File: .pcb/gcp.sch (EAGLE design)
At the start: 14 parts, among them SW1 POWER/COFFEE_SWITCHON-OFF

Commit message: Fixed steam lamp circuitry
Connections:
- net GREY: no longer STEAM_LAMP.2
- net N$2: now also STEAM_LAMP.2
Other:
- moved on the sheet: SSR-40DA1, STEAM_LAMP
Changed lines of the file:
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@@
 <attribute name="VALUE" x="-294.64" y="-64.77" size="1.778" layer="96" rot="R180"/>
 </instance>
-<instance part="STEAM_LAMP" gate="G$1" x="-274.32" y="-2.54" smashed="yes" rot="R90">
-<attribute name="NAME" x="-278.765" y="-5.08" size="1.778" layer="95" rot="R90"/>
-<attribute name="VALUE" x="-267.97" y="-5.08" size="1.778" layer="96" rot="R90"/>
+<instance part="STEAM_LAMP" gate="G$1" x="-231.14" y="0" smashed="yes" rot="R90">
+<attribute name="NAME" x="-235.585" y="-2.54" size="1.778" layer="95" rot="R90"/>
+<attribute name="VALUE" x="-224.79" y="-2.54" size="1.778" layer="96" rot="R90"/>
 </instance>
 <instance part="PUMP" gate="G$1" x="-187.96" y="5.08" smashed="yes" rot="R90">
@@
 <attribute name="VALUE" x="-215.9" y="22.86" size="1.778" layer="96" rot="R90"/>
 </instance>
-<instance part="SSR-40DA1" gate="G$1" x="-251.46" y="7.62" smashed="yes" rot="R90">
-<attribute name="NAME" x="-257.81" y="0" size="1.778" layer="95" font="vector" rot="R90"/>
+<instance part="SSR-40DA1" gate="G$1" x="-246.38" y="7.62" smashed="yes" rot="R90">
+<attribute name="NAME" x="-252.73" y="0" size="1.778" layer="95" font="vector" rot="R90"/>
 </instance>
 </instances>
@@
 <segment>
 <pinref part="SSR-40DA1" gate="G$1" pin="K"/>
-<wire x1="-248.92" y1="-2.54" x2="-248.92" y2="-5.08" width="0.1524" layer="91"/>
-<label x="-248.92" y="-5.08" size="1.778" layer="95" rot="R270"/>
+<wire x1="-243.84" y1="-2.54" x2="-243.84" y2="-5.08" width="0.1524" layer="91"/>
+<label x="-243.84" y="-5.08" size="1.778" layer="95" rot="R270"/>
 </segment>
 </net>
@@
 <segment>
 <pinref part="STEAM_LAMP" gate="G$1" pin="1"/>
-<wire x1="-274.32" y1="-15.24" x2="-274.32" y2="-7.62" width="0.1524" layer="91"/>
+<wire x1="-231.14" y1="-15.24" x2="-231.14" y2="-5.08" width="0.1524" layer="91"/>
 <pinref part="HEATER2" gate="G$1" pin="P$2"/>
-<wire x1="-261.62" y1="-15.24" x2="-274.32" y2="-15.24" width="0.1524" layer="91"/>
+<wire x1="-261.62" y1="-15.24" x2="-231.14" y2="-15.24" width="0.1524" layer="91"/>
 <wire x1="-254" y1="-27.94" x2="-254" y2="-33.02" width="0.1524" layer="91"/>
 <pinref part="HEATER1" gate="G$1" pin="P$2"/>
@@
 <pinref part="SSR-40DA" gate="G$1" pin="DS1"/>
 <wire x1="-259.08" y1="30.48" x2="-261.62" y2="30.48" width="0.1524" layer="91"/>
-<pinref part="STEAM_LAMP" gate="G$1" pin="2"/>
-<wire x1="-274.32" y1="5.08" x2="-274.32" y2="17.78" width="0.1524" layer="91"/>
 <pinref part="COFFEE_LAMP" gate="G$1" pin="1"/>
 <wire x1="-274.32" y1="27.94" x2="-274.32" y2="17.78" width="0.1524" layer="91"/>
@@
 <junction x="-261.62" y="17.78"/>
 <wire x1="-261.62" y1="17.78" x2="-274.32" y2="17.78" width="0.1524" layer="91"/>
-<junction x="-274.32" y="17.78"/>
-<wire x1="-254" y1="17.78" x2="-261.62" y2="17.78" width="0.1524" layer="91"/>
+<wire x1="-248.92" y1="17.78" x2="-261.62" y2="17.78" width="0.1524" layer="91"/>
 <pinref part="SSR-40DA1" gate="G$1" pin="DS1"/>
 </segment>
@@
 <segment>
 <pinref part="SSR-40DA1" gate="G$1" pin="A"/>
-<wire x1="-254" y1="-2.54" x2="-254" y2="-5.08" width="0.1524" layer="91"/>
-<label x="-256.54" y="-5.08" size="1.778" layer="95" rot="R270"/>
+<wire x1="-248.92" y1="-2.54" x2="-248.92" y2="-5.08" width="0.1524" layer="91"/>
+<label x="-251.46" y="-5.08" size="1.778" layer="95" rot="R270"/>
 </segment>
 </net>
@@
 <net name="N$2" class="0">
 <segment>
-<wire x1="-193.04" y1="17.78" x2="-248.92" y2="17.78" width="0.1524" layer="91"/>
+<wire x1="-193.04" y1="17.78" x2="-231.14" y2="17.78" width="0.1524" layer="91"/>
 <pinref part="U$4" gate="G$1" pin="4"/>
+<wire x1="-231.14" y1="17.78" x2="-243.84" y2="17.78" width="0.1524" layer="91"/>
 <wire x1="-200.66" y1="48.26" x2="-193.04" y2="48.26" width="0.1524" layer="91"/>
 <wire x1="-193.04" y1="48.26" x2="-193.04" y2="17.78" width="0.1524" layer="91"/>
 <pinref part="SSR-40DA1" gate="G$1" pin="DS2"/>
-</segment>
-</net>
+<pinref part="STEAM_LAMP" gate="G$1" pin="2"/>
+<wire x1="-231.14" y1="7.62" x2="-231.14" y2="17.78" width="0.1524" layer="91"/>
+<junction x="-231.14" y="17.78"/>
+</segment>
+</net>

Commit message: Nevermind.
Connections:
- net GREY: now also STEAM_LAMP.2
- net N$2: no longer STEAM_LAMP.2
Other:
- moved on the sheet: SSR-40DA1, STEAM_LAMP
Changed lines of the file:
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@@
 <attribute name="VALUE" x="-294.64" y="-64.77" size="1.778" layer="96" rot="R180"/>
 </instance>
-<instance part="STEAM_LAMP" gate="G$1" x="-231.14" y="0" smashed="yes" rot="R90">
-<attribute name="NAME" x="-235.585" y="-2.54" size="1.778" layer="95" rot="R90"/>
-<attribute name="VALUE" x="-224.79" y="-2.54" size="1.778" layer="96" rot="R90"/>
+<instance part="STEAM_LAMP" gate="G$1" x="-274.32" y="0" smashed="yes" rot="R90">
+<attribute name="NAME" x="-278.765" y="-2.54" size="1.778" layer="95" rot="R90"/>
+<attribute name="VALUE" x="-267.97" y="-2.54" size="1.778" layer="96" rot="R90"/>
 </instance>
 <instance part="PUMP" gate="G$1" x="-187.96" y="5.08" smashed="yes" rot="R90">
@@
 <attribute name="VALUE" x="-215.9" y="22.86" size="1.778" layer="96" rot="R90"/>
 </instance>
-<instance part="SSR-40DA1" gate="G$1" x="-246.38" y="7.62" smashed="yes" rot="R90">
-<attribute name="NAME" x="-252.73" y="0" size="1.778" layer="95" font="vector" rot="R90"/>
+<instance part="SSR-40DA1" gate="G$1" x="-248.92" y="7.62" smashed="yes" rot="R90">
+<attribute name="NAME" x="-255.27" y="0" size="1.778" layer="95" font="vector" rot="R90"/>
 </instance>
 </instances>
@@
 <segment>
 <pinref part="SSR-40DA1" gate="G$1" pin="K"/>
-<wire x1="-243.84" y1="-2.54" x2="-243.84" y2="-5.08" width="0.1524" layer="91"/>
-<label x="-243.84" y="-5.08" size="1.778" layer="95" rot="R270"/>
+<wire x1="-246.38" y1="-2.54" x2="-246.38" y2="-5.08" width="0.1524" layer="91"/>
+<label x="-246.38" y="-5.08" size="1.778" layer="95" rot="R270"/>
 </segment>
 </net>
@@
 <segment>
 <pinref part="STEAM_LAMP" gate="G$1" pin="1"/>
-<wire x1="-231.14" y1="-15.24" x2="-231.14" y2="-5.08" width="0.1524" layer="91"/>
+<wire x1="-274.32" y1="-15.24" x2="-274.32" y2="-5.08" width="0.1524" layer="91"/>
 <pinref part="HEATER2" gate="G$1" pin="P$2"/>
-<wire x1="-261.62" y1="-15.24" x2="-231.14" y2="-15.24" width="0.1524" layer="91"/>
+<wire x1="-261.62" y1="-15.24" x2="-274.32" y2="-15.24" width="0.1524" layer="91"/>
 <wire x1="-254" y1="-27.94" x2="-254" y2="-33.02" width="0.1524" layer="91"/>
 <pinref part="HEATER1" gate="G$1" pin="P$2"/>
@@
 <pinref part="SSR-40DA" gate="G$1" pin="DS1"/>
 <wire x1="-259.08" y1="30.48" x2="-261.62" y2="30.48" width="0.1524" layer="91"/>
+<pinref part="STEAM_LAMP" gate="G$1" pin="2"/>
+<wire x1="-274.32" y1="7.62" x2="-274.32" y2="17.78" width="0.1524" layer="91"/>
 <pinref part="COFFEE_LAMP" gate="G$1" pin="1"/>
 <wire x1="-274.32" y1="27.94" x2="-274.32" y2="17.78" width="0.1524" layer="91"/>
@@
 <junction x="-261.62" y="17.78"/>
 <wire x1="-261.62" y1="17.78" x2="-274.32" y2="17.78" width="0.1524" layer="91"/>
-<wire x1="-248.92" y1="17.78" x2="-261.62" y2="17.78" width="0.1524" layer="91"/>
+<junction x="-274.32" y="17.78"/>
+<wire x1="-251.46" y1="17.78" x2="-261.62" y2="17.78" width="0.1524" layer="91"/>
 <pinref part="SSR-40DA1" gate="G$1" pin="DS1"/>
 </segment>
@@
 <segment>
 <pinref part="SSR-40DA1" gate="G$1" pin="A"/>
-<wire x1="-248.92" y1="-2.54" x2="-248.92" y2="-5.08" width="0.1524" layer="91"/>
-<label x="-251.46" y="-5.08" size="1.778" layer="95" rot="R270"/>
+<wire x1="-251.46" y1="-2.54" x2="-251.46" y2="-5.08" width="0.1524" layer="91"/>
+<label x="-254" y="-5.08" size="1.778" layer="95" rot="R270"/>
 </segment>
 </net>
@@
 <net name="N$2" class="0">
 <segment>
-<wire x1="-193.04" y1="17.78" x2="-231.14" y2="17.78" width="0.1524" layer="91"/>
+<wire x1="-193.04" y1="17.78" x2="-246.38" y2="17.78" width="0.1524" layer="91"/>
 <pinref part="U$4" gate="G$1" pin="4"/>
-<wire x1="-231.14" y1="17.78" x2="-243.84" y2="17.78" width="0.1524" layer="91"/>
 <wire x1="-200.66" y1="48.26" x2="-193.04" y2="48.26" width="0.1524" layer="91"/>
 <wire x1="-193.04" y1="48.26" x2="-193.04" y2="17.78" width="0.1524" layer="91"/>
 <pinref part="SSR-40DA1" gate="G$1" pin="DS2"/>
-<pinref part="STEAM_LAMP" gate="G$1" pin="2"/>
-<wire x1="-231.14" y1="7.62" x2="-231.14" y2="17.78" width="0.1524" layer="91"/>
-<junction x="-231.14" y="17.78"/>
-</segment>
-</net>
+</segment>
+</net>

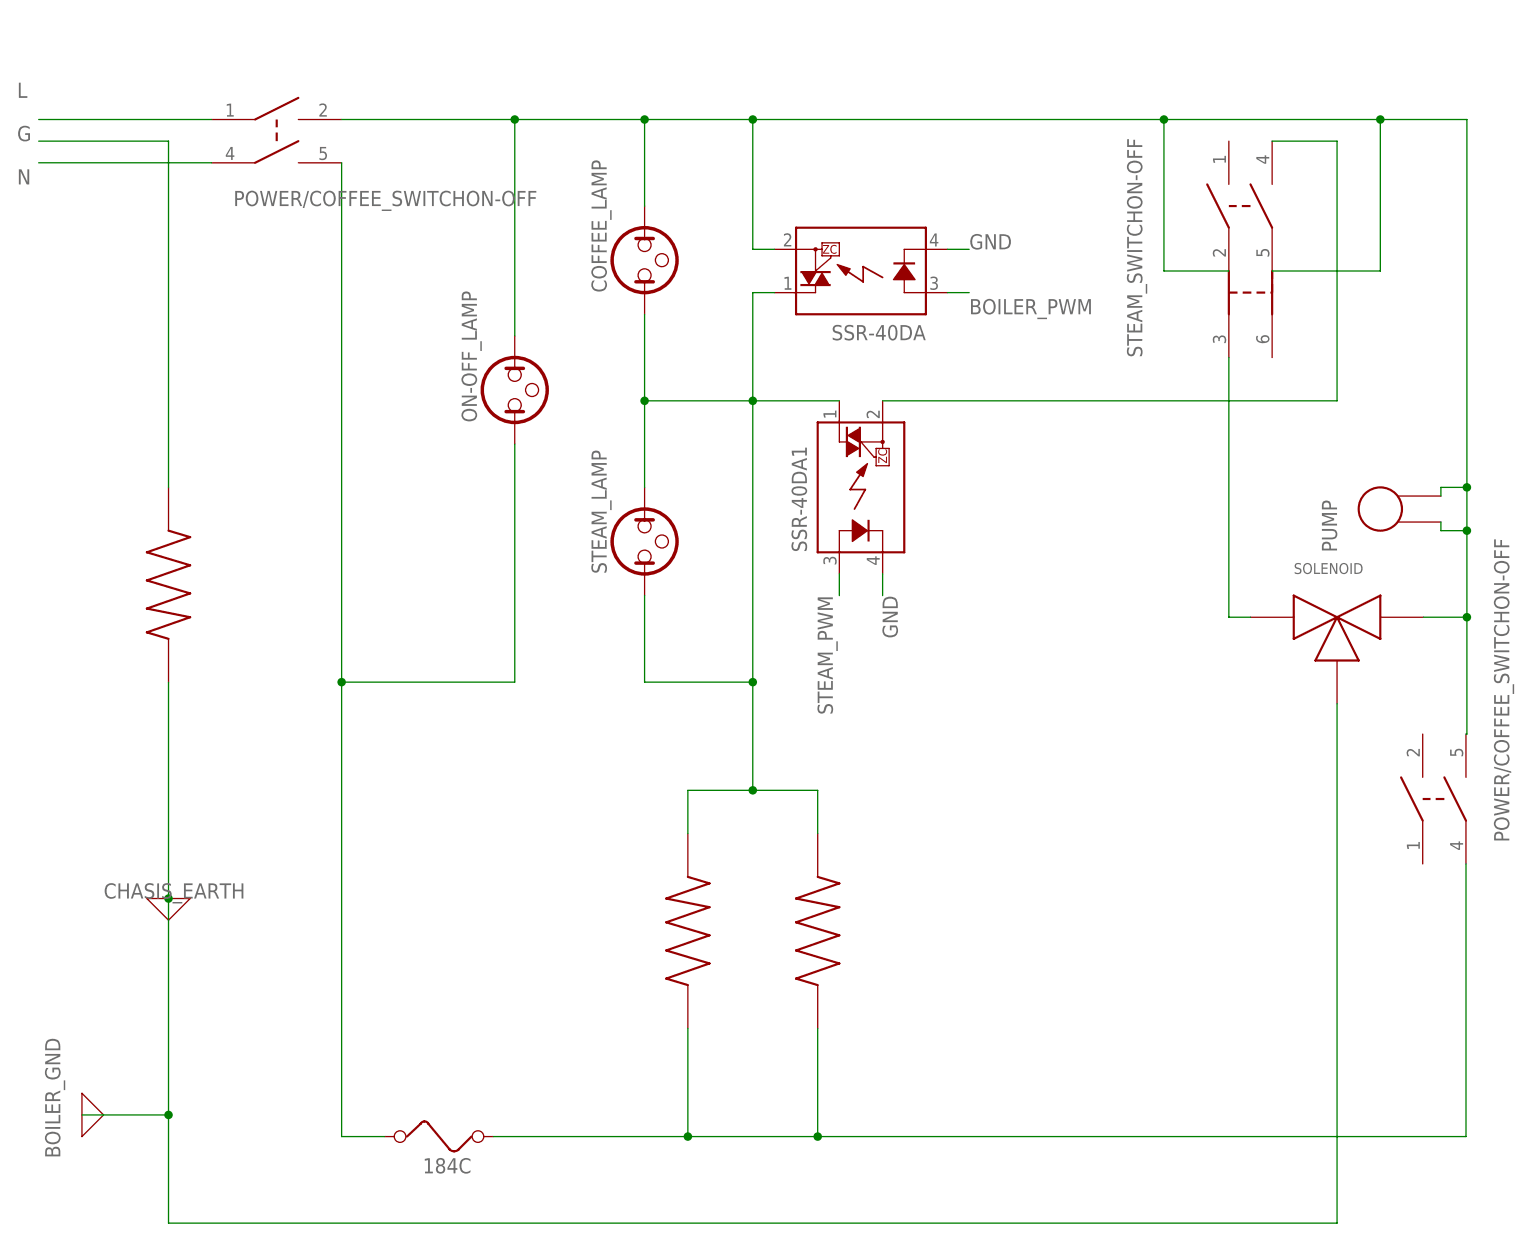
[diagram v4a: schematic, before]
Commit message: Increase readability of schematic
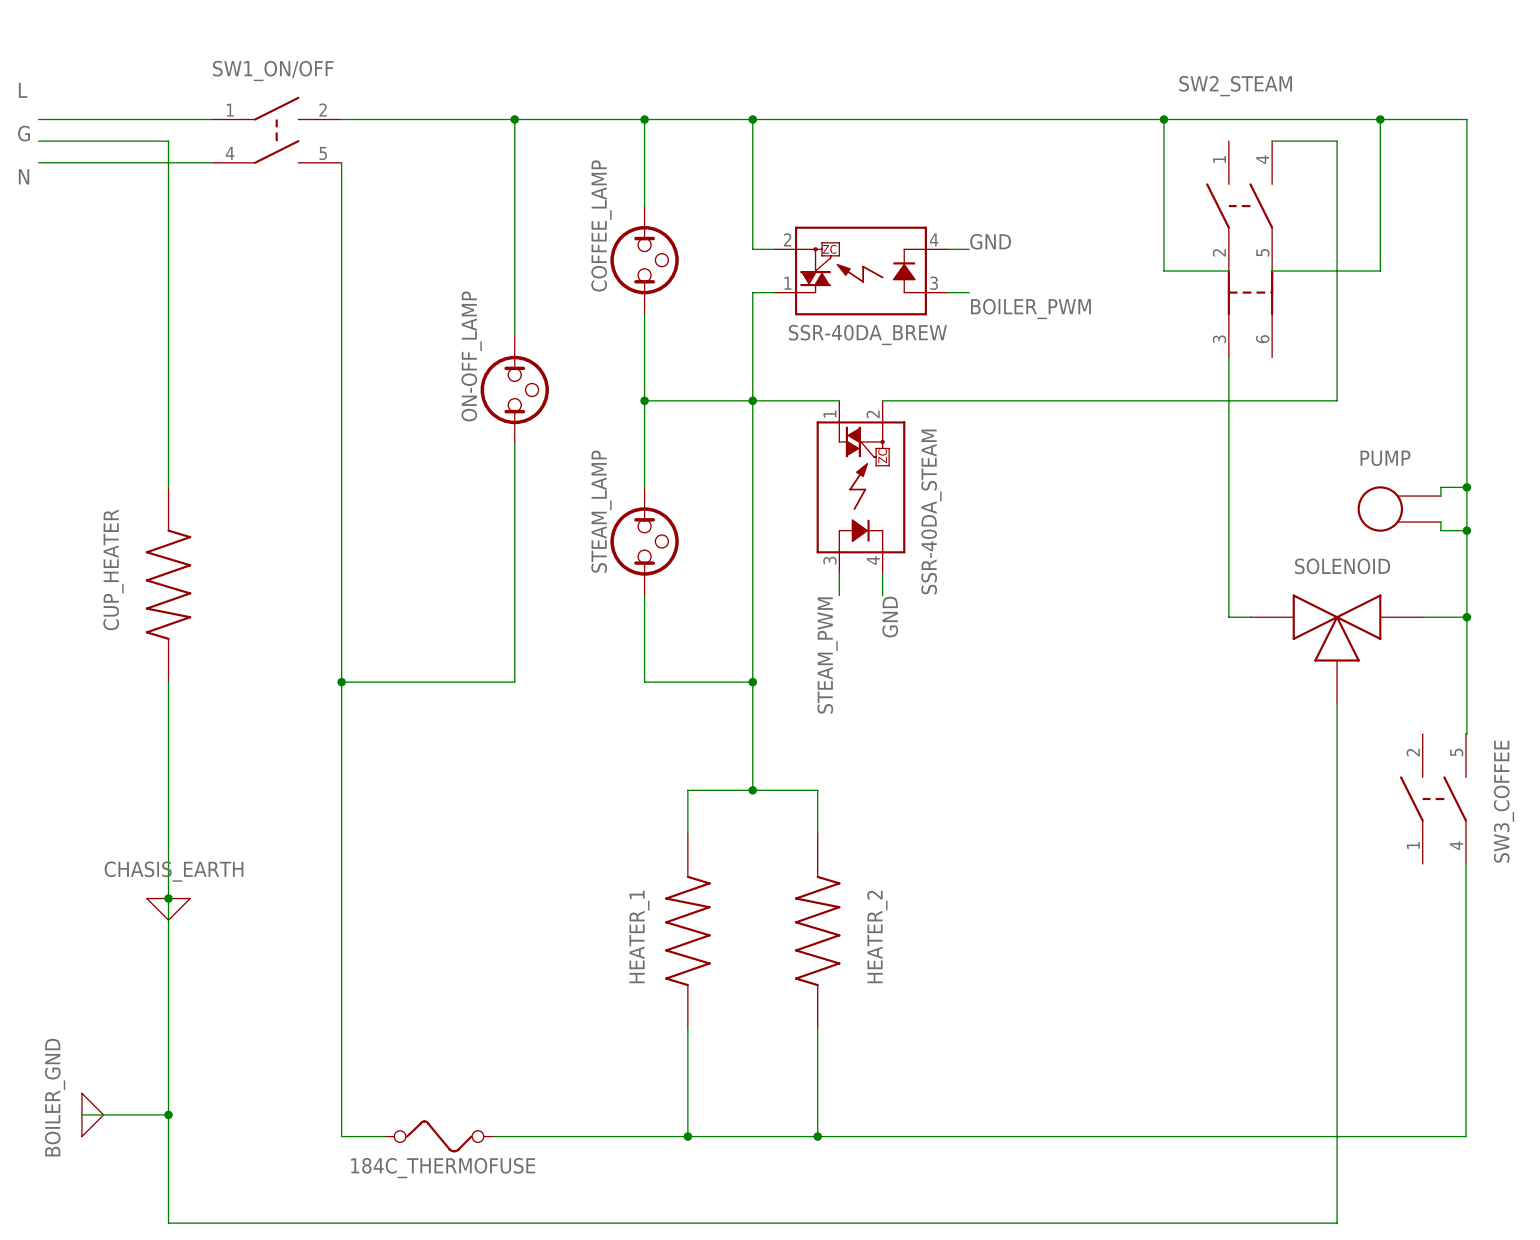
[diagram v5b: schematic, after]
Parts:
- renumbered 184C to 184C_THERMOFUSE, HEATER1 to HEATER_1, HEATER2 to HEATER_2, SSR-40DA to SSR-40DA_BREW, SSR-40DA1 to SSR-40DA_STEAM, SW1 to SW1_ON/OFF, U$3 to SW3_COFFEE, U$4 to SW2_STEAM

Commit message: Add labels and fix wiring schematic
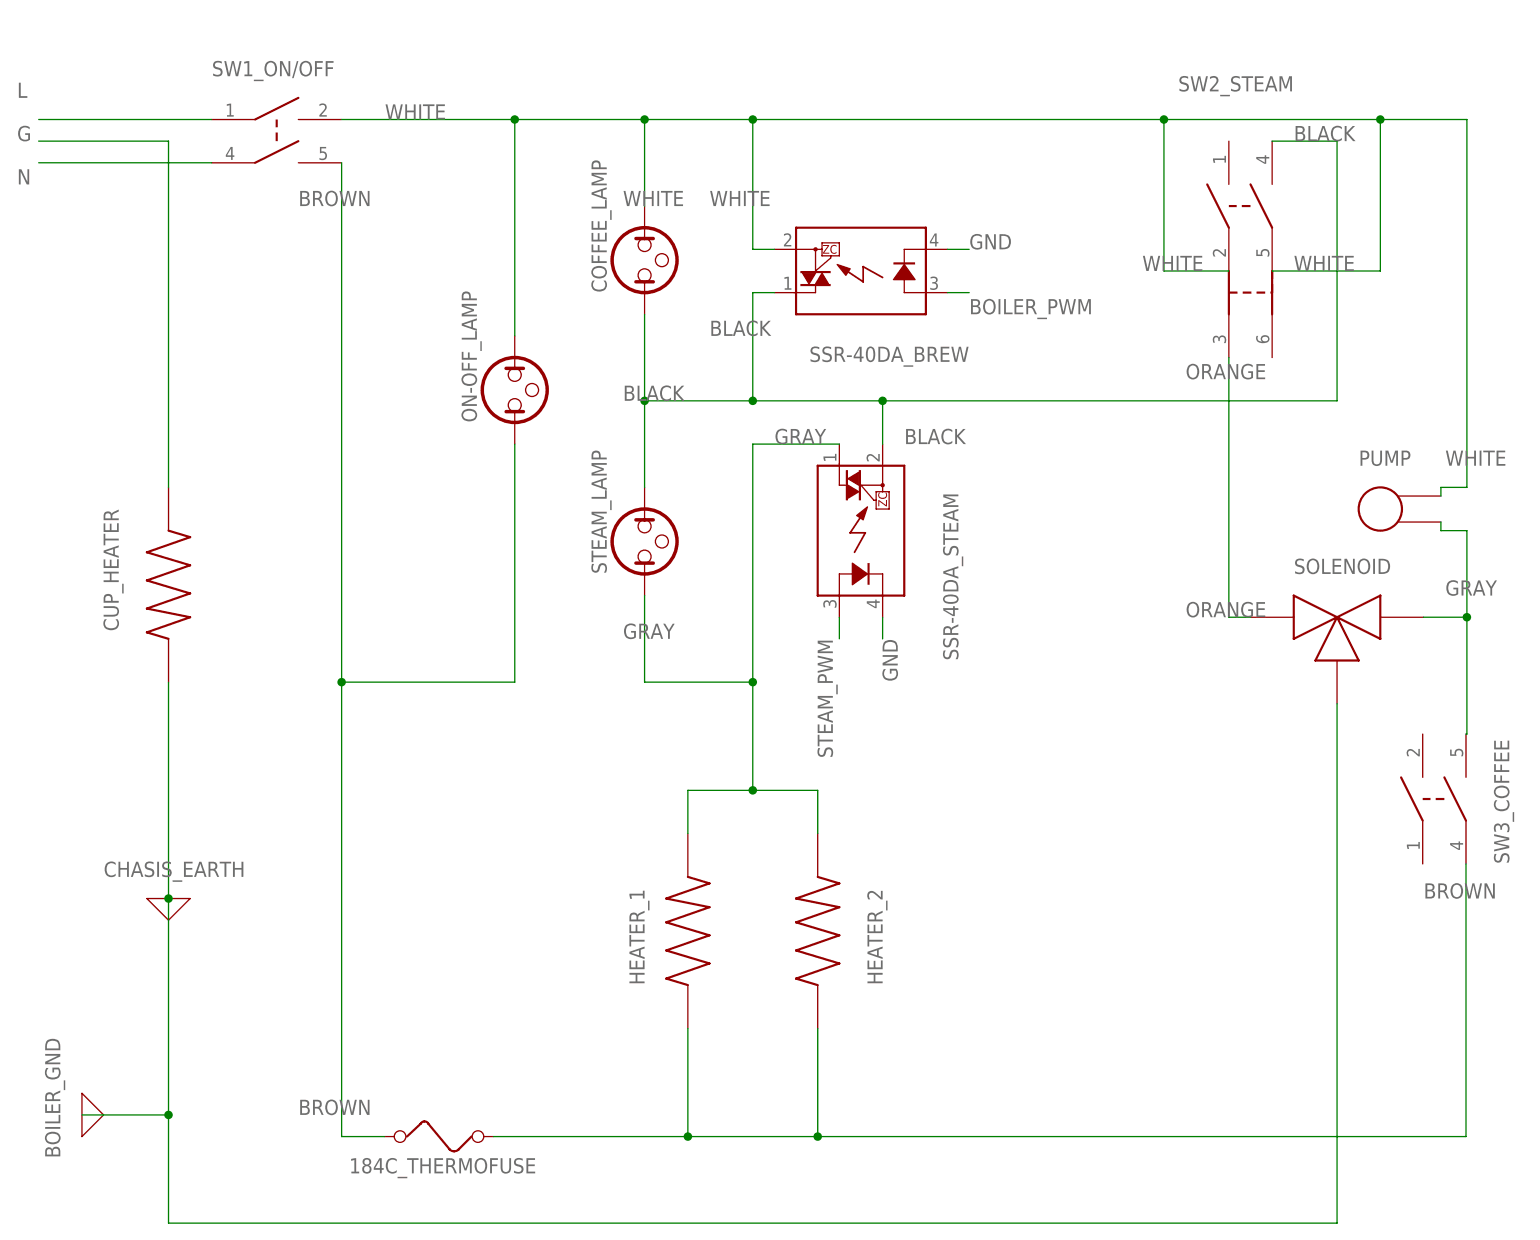
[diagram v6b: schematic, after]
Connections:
- net N$1 renamed ORANGE
- removed net GREY: COFFEE_LAMP.1, HEATER_1.P$2, HEATER_2.P$2, SSR-40DA_BREW.DS1, SSR-40DA_STEAM.DS1, STEAM_LAMP.1, STEAM_LAMP.2
- removed net N$2: SSR-40DA_STEAM.DS2, SW2_STEAM.4
- removed net N$6: 184C_THERMOFUSE.1, HEATER_1.P$1, HEATER_2.P$1, SW3_COFFEE.5
- new net BLACK: COFFEE_LAMP.1, SSR-40DA_BREW.DS1, SSR-40DA_STEAM.DS2, STEAM_LAMP.2, SW2_STEAM.4
- new net GRAY: HEATER_1.P$2, HEATER_2.P$2, NORMALLY_OPEN.P$2, PUMP.P$1, SSR-40DA_STEAM.DS1, STEAM_LAMP.1, SW3_COFFEE.4
- net BROWN: now also 184C_THERMOFUSE.1, HEATER_1.P$1, HEATER_2.P$1, SW3_COFFEE.5
- net WHITE: no longer NORMALLY_OPEN.P$2, PUMP.P$1, SW3_COFFEE.4
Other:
- moved on the sheet: SSR-40DA_STEAM
